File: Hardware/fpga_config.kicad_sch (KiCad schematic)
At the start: 11 parts, among them Q1 2N7002, U1 NC7SZ125M5X, U2 XC7A35T-CSG325, U3 FT232H

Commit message: I gotta find the right regulators
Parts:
- C5: footprint (none) -> Capacitor_SMD:C_01005_0402Metric
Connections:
- net LGA_CLK4_N: now reaches U2.C13 (IO_L11N_T1_SRCC_15)
- net LGA_CLK4_P: now reaches U2.D13 (IO_L11P_T1_SRCC_15)
- net LGA_CLK5_N: now reaches U2.D14 (IO_L12N_T1_MRCC_15)
- net LGA_CLK6_N: now reaches U2.D15 (IO_L13N_T2_MRCC_15)
- net LGA_CLK7_N: now reaches U2.D16 (IO_L14N_T2_SRCC_15)
- net LGA_CLK5_P: now reaches U2.E13 (IO_L12P_T1_MRCC_15)
- net LGA_CLK6_P: now reaches U2.E15 (IO_L13P_T2_MRCC_15)
- net LGA_CLK7_P: now reaches U2.E16 (IO_L14P_T2_SRCC_15)
- net +3V3 renamed +2V5
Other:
- moved on the sheet: R3, U2A

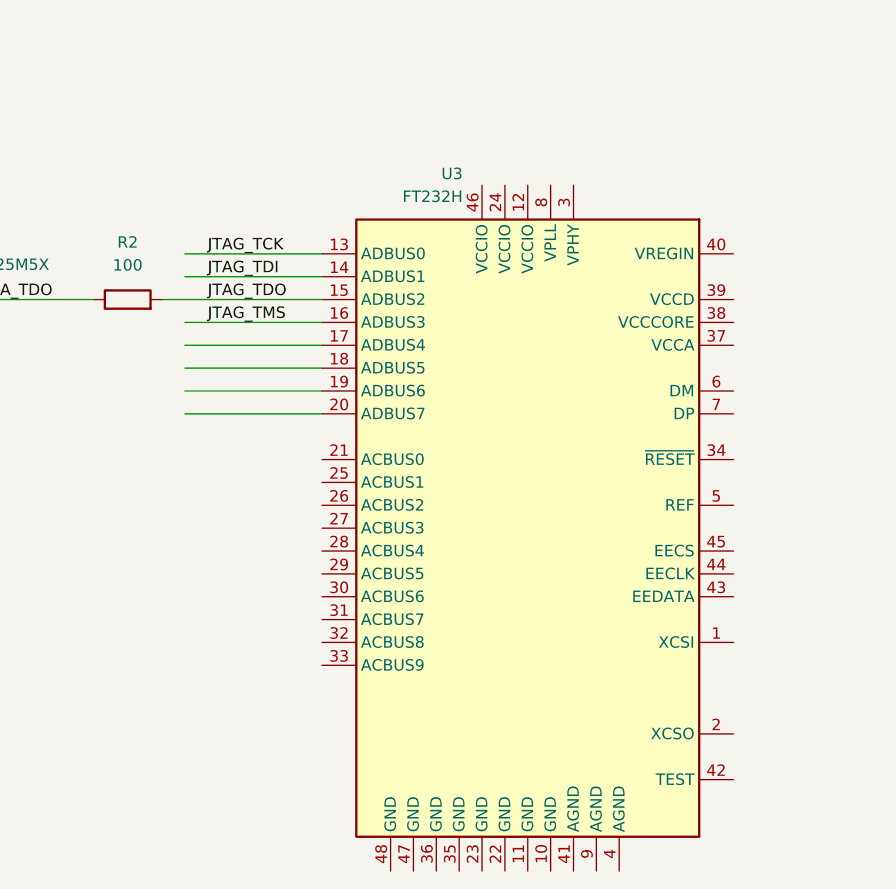
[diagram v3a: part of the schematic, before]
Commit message: Filling out the JTAG
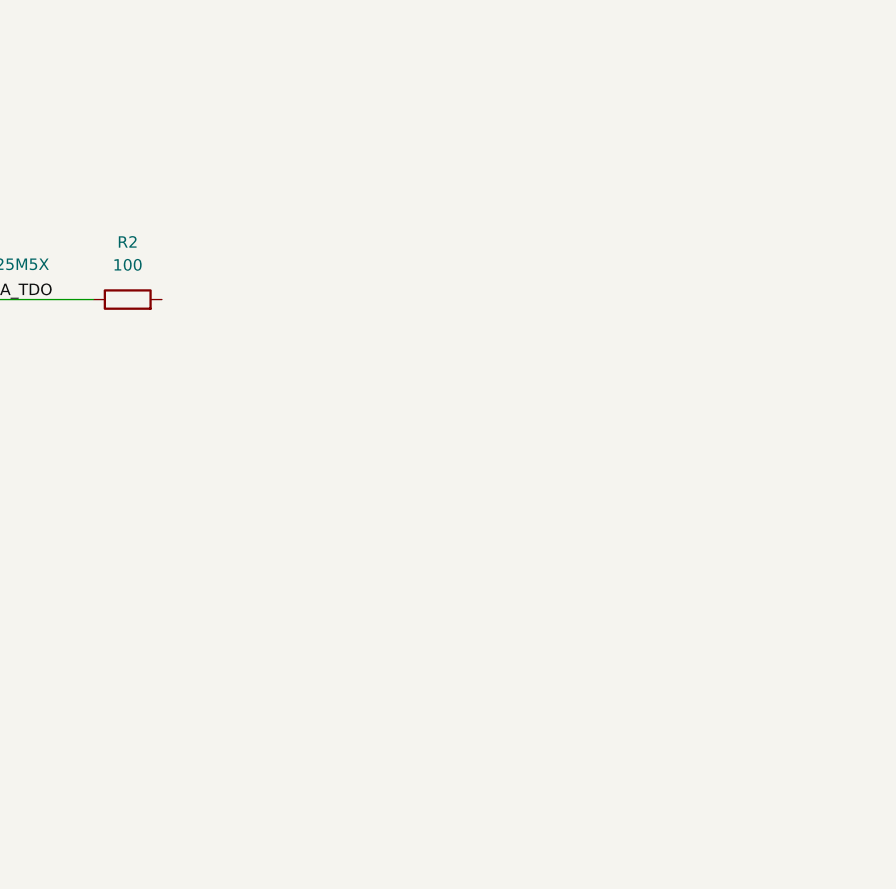
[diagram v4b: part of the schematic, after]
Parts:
- removed U3: FT232H, Package_QFP:LQFP-48_7x7mm_P0.5mm, symbol Interface_USB:FT232H
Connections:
- net JTAG_TDO: no longer names the net of R2.2
